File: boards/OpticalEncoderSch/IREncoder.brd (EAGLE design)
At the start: 25.4 x 25.4 mm, 12 parts, among them J1 3_PIN_JST-XH

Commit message: Optical Encoder PCB updates. Awaits peer review and shipment
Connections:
- removed net N$7: J1.P$3
- net GND: now also J1.P$3
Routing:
- net +5V: track 49.8 -> 67.7 mm, vias 2 -> 3
- net N$5: track 7.24 -> 23.2 mm, vias 0 -> 1
- net N$3: track 3.81 -> 4.58 mm
- net N$1: track 3.81 -> 4.58 mm
- added copper zone on layer 1, net GND
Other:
- board text added: "10K"
- board text added: "470"
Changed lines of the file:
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@@
 <hole x="23.495" y="1.905" drill="3.175"/>
 <hole x="23.495" y="23.495" drill="3.175"/>
+<text x="23.622" y="20.066" size="0.508" layer="21">470</text>
+<text x="23.622" y="16.764" size="0.508" layer="21">470</text>
+<text x="0.762" y="8.128" size="0.508" layer="21">470</text>
+<text x="0.762" y="4.826" size="0.508" layer="21">470</text>
+<text x="23.622" y="8.128" size="0.508" layer="21">10K</text>
+<text x="23.622" y="5.08" size="0.508" layer="21">10K</text>
 </plain>
 <attributes>
@@
 <contactref element="R6" pad="2"/>
 <contactref element="J1" pad="P$1"/>
-<wire x1="4.13" y1="5.08" x2="6.03" y2="6.98" width="0.254" layer="1"/>
-<wire x1="6.03" y1="6.98" x2="6.03" y2="8.255" width="0.254" layer="1"/>
-<wire x1="21.27" y1="20.32" x2="19.05" y2="18.1" width="0.254" layer="1"/>
-<wire x1="19.05" y1="18.1" x2="19.05" y2="17.78" width="0.254" layer="1"/>
-<wire x1="4.13" y1="5.08" x2="1.27" y2="5.08" width="0.254" layer="1"/>
 <wire x1="21.27" y1="20.32" x2="22.86" y2="20.32" width="0.254" layer="1"/>
 <via x="22.86" y="20.32" extent="1-16" drill="0.35"/>
-<wire x1="22.86" y1="20.32" x2="22.86" y2="6.35" width="0.254" layer="16"/>
-<wire x1="22.86" y1="6.35" x2="24.13" y2="5.08" width="0.254" layer="16"/>
+<wire x1="22.86" y1="20.32" x2="22.86" y2="5.08" width="0.254" layer="16"/>
 <wire x1="15.24" y1="1.27" x2="19.05" y2="5.08" width="0.254" layer="16"/>
 <wire x1="15.24" y1="1.27" x2="8.89" y2="1.27" width="0.254" layer="16"/>
 <wire x1="8.89" y1="1.27" x2="5.08" y2="5.08" width="0.254" layer="16"/>
-<via x="24.13" y="5.08" extent="1-16" drill="0.35"/>
-<wire x1="19.05" y1="5.08" x2="24.13" y2="5.08" width="0.254" layer="16"/>
-<wire x1="19.05" y1="17.78" x2="19.37" y2="17.145" width="0" layer="19" extent="1-1"/>
-<wire x1="4.13" y1="5.08" x2="5.08" y2="5.08" width="0" layer="19" extent="1-16"/>
-<wire x1="21.27" y1="5.08" x2="19.05" y2="5.08" width="0" layer="19" extent="1-16"/>
-<wire x1="7.845" y1="17.69" x2="6.03" y2="8.255" width="0" layer="19" extent="1-1"/>
+<via x="22.86" y="5.08" extent="1-16" drill="0.35"/>
+<wire x1="19.05" y1="5.08" x2="22.86" y2="5.08" width="0.254" layer="16"/>
+<via x="2.54" y="5.08" extent="1-16" drill="0.35"/>
+<wire x1="2.54" y1="5.08" x2="2.54" y2="14.732" width="0.254" layer="16"/>
+<wire x1="2.54" y1="14.732" x2="5.588" y2="17.78" width="0.254" layer="16"/>
+<wire x1="7.755" y1="17.78" x2="7.845" y2="17.69" width="0.254" layer="16"/>
+<wire x1="5.588" y1="17.78" x2="7.755" y2="17.78" width="0.254" layer="16"/>
+<wire x1="21.27" y1="5.08" x2="22.86" y2="5.08" width="0.254" layer="1"/>
+<wire x1="5.08" y1="5.08" x2="2.54" y2="5.08" width="0.254" layer="16"/>
+<wire x1="4.13" y1="5.08" x2="2.54" y2="5.08" width="0.254" layer="1"/>
+<wire x1="5.842" y1="8.067" x2="6.03" y2="8.255" width="0.254" layer="1"/>
+<wire x1="4.13" y1="5.08" x2="4.318" y2="5.268" width="0.254" layer="1"/>
+<wire x1="4.318" y1="5.268" x2="4.318" y2="6.096" width="0.254" layer="1"/>
+<wire x1="4.318" y1="6.096" x2="5.842" y2="7.62" width="0.254" layer="1"/>
+<wire x1="5.842" y1="7.62" x2="5.842" y2="8.067" width="0.254" layer="1"/>
+<wire x1="19.37" y1="17.145" x2="19.558" y2="17.333" width="0.254" layer="1"/>
+<wire x1="19.558" y1="17.333" x2="19.558" y2="18.288" width="0.254" layer="1"/>
+<wire x1="19.558" y1="18.288" x2="21.27" y2="20" width="0.254" layer="1"/>
+<wire x1="21.27" y1="20" x2="21.27" y2="20.32" width="0.254" layer="1"/>
 </signal>
 <signal name="N$5">
@@
 <contactref element="D5" pad="A"/>
 <contactref element="J1" pad="P$2"/>
-<wire x1="13.97" y1="12.7" x2="18.415" y2="8.255" width="0.254" layer="1"/>
+<wire x1="13.97" y1="12.7" x2="17.018" y2="9.652" width="0.254" layer="1"/>
+<wire x1="17.018" y1="9.652" x2="18.415" y2="8.255" width="0.254" layer="1"/>
 <wire x1="18.415" y1="8.255" x2="19.37" y2="8.255" width="0.254" layer="1"/>
-<wire x1="13.97" y1="12.7" x2="7.845" y2="20.19" width="0" layer="19" extent="1-1"/>
+<via x="17.018" y="9.652" extent="1-16" drill="0.35"/>
+<wire x1="7.845" y1="20.19" x2="11.779" y2="16.256" width="0.254" layer="16"/>
+<wire x1="14.478" y1="16.256" x2="17.018" y2="13.716" width="0.254" layer="16"/>
+<wire x1="17.018" y1="13.716" x2="17.018" y2="9.652" width="0.254" layer="16"/>
+<wire x1="11.779" y1="16.256" x2="14.478" y2="16.256" width="0.254" layer="16"/>
 </signal>
 <signal name="N$6">
@@
 <contactref element="D1" pad="K"/>
 <contactref element="D5" pad="K"/>
-<wire x1="11.43" y1="12.7" x2="19.05" y2="12.7" width="0" layer="19" extent="1-1"/>
-<wire x1="6.35" y1="12.7" x2="11.43" y2="12.7" width="0" layer="19" extent="1-1"/>
-<wire x1="11.43" y1="20.32" x2="11.43" y2="12.7" width="0" layer="19" extent="1-1"/>
-<wire x1="13.97" y1="5.08" x2="11.43" y2="12.7" width="0" layer="19" extent="1-1"/>
+<contactref element="J1" pad="P$3"/>
+<polygon width="0.254" layer="1" isolate="0.4064">
+<vertex x="0" y="25.4"/>
+<vertex x="0" y="0"/>
+<vertex x="25.4" y="0"/>
+<vertex x="25.4" y="25.4"/>
+</polygon>
 </signal>
 <signal name="N$1">
 <contactref element="R4" pad="1"/>
 <contactref element="D4" pad="A"/>
-<wire x1="21.59" y1="12.7" x2="21.59" y2="16.51" width="0.254" layer="1"/>
-<wire x1="21.59" y1="16.51" x2="21.27" y2="17.145" width="0" layer="19" extent="1-1"/>
+<wire x1="21.27" y1="17.145" x2="21.27" y2="13.02" width="0.254" layer="1"/>
+<wire x1="21.27" y1="13.02" x2="21.59" y2="12.7" width="0.254" layer="1"/>
 </signal>
 <signal name="N$2">
@@
 <contactref element="R2" pad="1"/>
 <contactref element="D2" pad="A"/>
-<wire x1="3.81" y1="12.7" x2="3.81" y2="8.89" width="0.254" layer="1"/>
-<wire x1="3.81" y1="8.89" x2="4.13" y2="8.255" width="0" layer="19" extent="1-1"/>
+<wire x1="4.13" y1="8.255" x2="4.13" y2="12.38" width="0.254" layer="1"/>
+<wire x1="4.13" y1="12.38" x2="3.81" y2="12.7" width="0.254" layer="1"/>
 </signal>
 <signal name="N$4">
@@
 <wire x1="11.43" y1="5.08" x2="6.03" y2="5.08" width="0.254" layer="1"/>
 </signal>
-<signal name="N$7">
-<contactref element="J1" pad="P$3"/>
-</signal>
-<signal name="N$8">
-<via x="1.27" y="5.08" extent="1-16" drill="0.35"/>
-</signal>
 </signals>

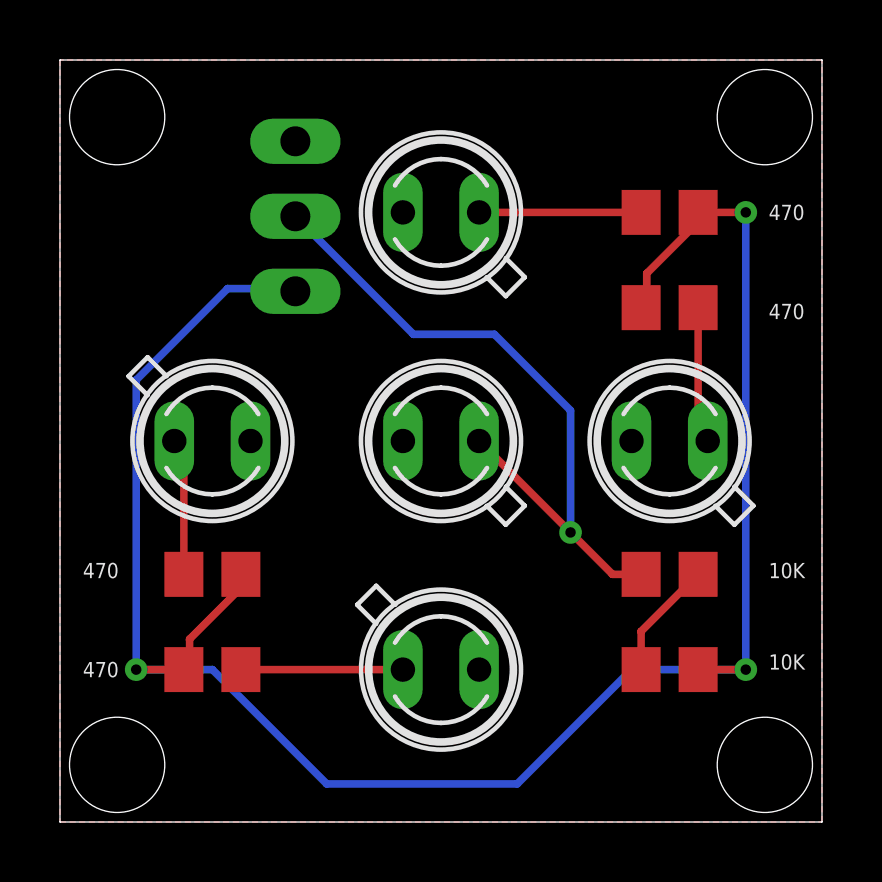
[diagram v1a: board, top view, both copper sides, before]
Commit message: Updating encoder board to fix clearance issues and voltage level
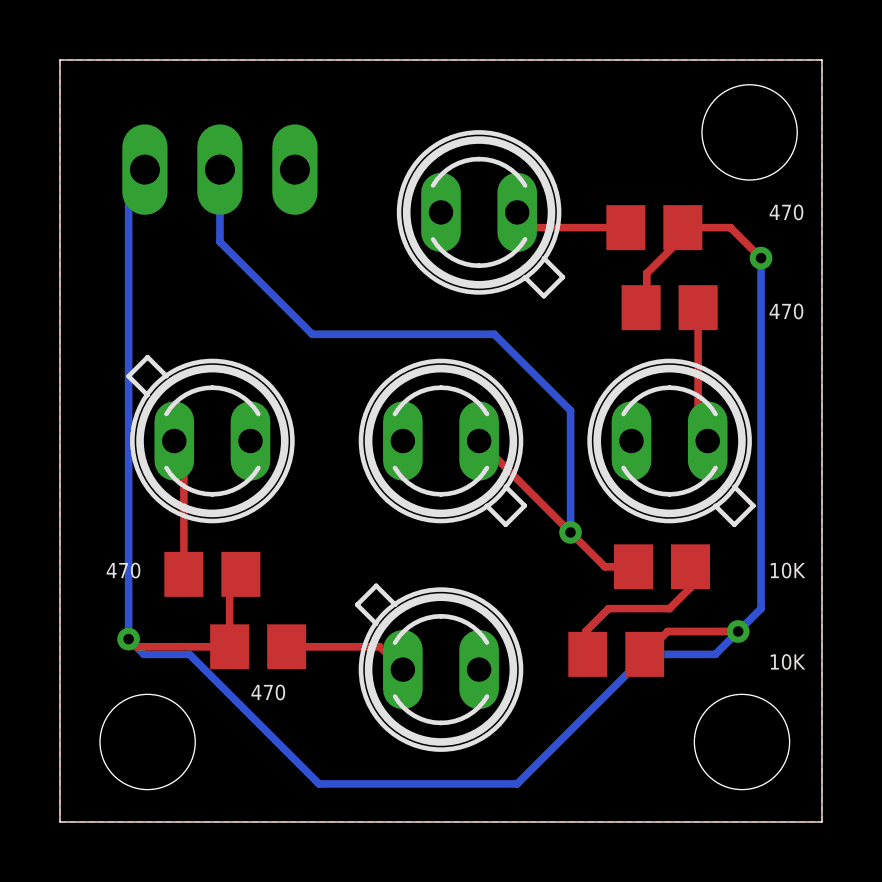
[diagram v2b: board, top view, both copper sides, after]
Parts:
- moved J1 10.7 mm to (0.38, 25.1), turned to 180 degrees
- moved R6 1.85 mm to (18.5, 5.59)
- moved R1 1.70 mm to (6.60, 5.84)
- moved D3 1.27 mm to (14.0, 20.3)
- moved R3 0.72 mm to (19.8, 19.8)
- moved R5 0.36 mm to (20.1, 8.51)
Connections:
- net +5V renamed +3V3
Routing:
- net N$5: track 23.2 -> 27.4 mm
- net +3V3: track 67.7 -> 69.3 mm
- net N$6: track 3.96 -> 5.58 mm
- net N$2: track 5.40 -> 3.83 mm
- net N$4: track 5.40 -> 4.19 mm

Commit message: Cleaning up routing and labels for design review
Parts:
- moved R4 1.27 mm to (21.6, 17.1)
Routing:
- net N$5: track 27.4 -> 21.7 mm, vias 1 -> 0
- net +3V3: track 69.3 -> 69.9 mm
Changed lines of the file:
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@@
 <attribute name="SPICEPREFIX" value="R" x="41.402" y="-4.318" size="1.778" layer="27" display="off"/>
 </element>
-<element name="R4" library="rcl" library_urn="urn:adsk.eagle:library:334" package="R0805" package3d_urn="urn:adsk.eagle:package:23553/2" value="470" x="20.32" y="17.145" smashed="yes" rot="R180">
-<attribute name="SPICEPREFIX" value="R" x="-6.35" y="41.275" size="1.778" layer="27" rot="R180" display="off"/>
+<element name="R4" library="rcl" library_urn="urn:adsk.eagle:library:334" package="R0805" package3d_urn="urn:adsk.eagle:package:23553/2" value="470" x="21.59" y="17.145" smashed="yes" rot="R180">
+<attribute name="SPICEPREFIX" value="R" x="-5.08" y="41.275" size="1.778" layer="27" rot="R180" display="off"/>
 </element>
 <element name="R5" library="rcl" library_urn="urn:adsk.eagle:library:334" package="R0805" package3d_urn="urn:adsk.eagle:package:23553/2" value="10k" x="20.066" y="8.509" smashed="yes">
@@
 <contactref element="D5" pad="A"/>
 <contactref element="J1" pad="P$2"/>
-<wire x1="13.97" y1="12.7" x2="17.018" y2="9.652" width="0.254" layer="1"/>
-<wire x1="17.018" y1="9.652" x2="18.161" y2="8.509" width="0.254" layer="1"/>
+<wire x1="13.97" y1="12.7" x2="18.161" y2="8.509" width="0.254" layer="1"/>
 <wire x1="18.161" y1="8.509" x2="19.116" y2="8.509" width="0.254" layer="1"/>
-<via x="17.018" y="9.652" extent="1-16" drill="0.35"/>
-<wire x1="14.478" y1="16.256" x2="17.018" y2="13.716" width="0.254" layer="16"/>
-<wire x1="17.018" y1="13.716" x2="17.018" y2="9.652" width="0.254" layer="16"/>
-<wire x1="14.478" y1="16.256" x2="8.41168125" y2="16.256" width="0.254" layer="16"/>
-<wire x1="8.41168125" y1="16.256" x2="5.331" y2="19.33668125" width="0.254" layer="16"/>
+<wire x1="5.331" y1="19.33668125" x2="8.41168125" y2="16.256" width="0.254" layer="16"/>
 <wire x1="5.331" y1="19.33668125" x2="5.331" y2="21.746" width="0.254" layer="16"/>
+<wire x1="8.41168125" y1="16.256" x2="12.192" y2="16.256" width="0.254" layer="16"/>
+<wire x1="12.192" y1="16.256" x2="13.97" y2="14.478" width="0.254" layer="16"/>
+<wire x1="13.97" y1="14.478" x2="13.97" y2="12.7" width="0.254" layer="16"/>
 </signal>
 <signal name="N$6">
@@
 <contactref element="R4" pad="1"/>
 <contactref element="D4" pad="A"/>
-<wire x1="21.27" y1="17.145" x2="21.27" y2="13.02" width="0.254" layer="1"/>
-<wire x1="21.27" y1="13.02" x2="21.59" y2="12.7" width="0.254" layer="1"/>
+<wire x1="22.54" y1="17.145" x2="22.54" y2="13.65" width="0.254" layer="1"/>
+<wire x1="21.59" y1="12.7" x2="22.54" y2="13.65" width="0.254" layer="1"/>
 </signal>
 <signal name="N$2">
@@
 <contactref element="R2" pad="2"/>
 <contactref element="R1" pad="2"/>
-<wire x1="19.37" y1="17.145" x2="19.558" y2="17.333" width="0.254" layer="1"/>
-<wire x1="19.558" y1="17.333" x2="19.558" y2="18.288" width="0.254" layer="1"/>
-<wire x1="19.558" y1="18.288" x2="20.762" y2="19.492" width="0.254" layer="1"/>
-<wire x1="20.762" y1="19.492" x2="20.762" y2="19.812" width="0.254" layer="1"/>
+<wire x1="20.762" y1="17.9862" x2="20.64" y2="17.785" width="0.254" layer="1"/>
+<wire x1="20.64" y1="17.145" x2="20.64" y2="17.785" width="0.254" layer="1"/>
+<wire x1="20.762" y1="17.9862" x2="20.762" y2="19.812" width="0.254" layer="1"/>
 <wire x1="5.654" y1="5.842" x2="5.654" y2="7.879" width="0.254" layer="1"/>
 <wire x1="5.654" y1="7.879" x2="6.03" y2="8.255" width="0.254" layer="1"/>
@@
 <wire x1="15.24" y1="1.27" x2="19.558" y2="5.588" width="0.254" layer="16"/>
 <wire x1="15.24" y1="1.27" x2="8.636" y2="1.27" width="0.254" layer="16"/>
-<wire x1="8.636" y1="1.27" x2="4.318" y2="5.588" width="0.254" layer="16"/>
-<wire x1="4.318" y1="5.588" x2="2.794" y2="5.588" width="0.254" layer="16"/>
-<wire x1="2.794" y1="5.588" x2="2.286" y2="6.096" width="0.254" layer="16"/>
+<wire x1="8.636" y1="1.27" x2="4.064" y2="5.842" width="0.254" layer="16"/>
+<wire x1="4.064" y1="5.842" x2="2.794" y2="5.842" width="0.254" layer="16"/>
+<wire x1="2.794" y1="5.842" x2="1.778" y2="6.858" width="0.254" layer="16"/>
 <via x="22.606" y="6.35" extent="1-16" drill="0.35"/>
 <wire x1="21.844" y1="5.588" x2="22.606" y2="6.35" width="0.254" layer="16"/>
 <wire x1="21.844" y1="5.588" x2="19.558" y2="5.588" width="0.254" layer="16"/>
-<via x="2.286" y="6.096" extent="1-16" drill="0.35"/>
-<wire x1="22.606" y1="6.35" x2="20.254" y2="6.35" width="0.254" layer="1"/>
+<via x="1.778" y="6.858" extent="1-16" drill="0.35"/>
+<wire x1="22.606" y1="6.35" x2="21.844" y2="5.588" width="0.254" layer="1"/>
+<wire x1="21.844" y1="5.588" x2="19.492" y2="5.588" width="0.254" layer="1"/>
 <wire x1="6.03" y1="8.26" x2="5.654" y2="8.636" width="0.254" layer="1"/>
-<wire x1="2.286" y1="21.201" x2="2.831" y2="21.746" width="0.254" layer="16"/>
-<wire x1="2.286" y1="6.096" x2="2.286" y2="21.201" width="0.254" layer="16"/>
-<wire x1="20.254" y1="6.35" x2="19.492" y2="5.588" width="0.254" layer="1"/>
+<wire x1="1.778" y1="20.693" x2="2.831" y2="21.746" width="0.254" layer="16"/>
+<wire x1="1.778" y1="6.858" x2="1.778" y2="20.693" width="0.254" layer="16"/>
 <wire x1="22.352" y1="19.812" x2="20.762" y2="19.812" width="0.254" layer="1"/>
-<wire x1="2.286" y1="6.096" x2="2.54" y2="5.842" width="0.254" layer="1"/>
-<wire x1="2.54" y1="5.842" x2="5.654" y2="5.842" width="0.254" layer="1"/>
+<wire x1="1.778" y1="6.858" x2="2.794" y2="5.842" width="0.254" layer="1"/>
+<wire x1="2.794" y1="5.842" x2="5.654" y2="5.842" width="0.254" layer="1"/>
 <wire x1="6.03" y1="8.255" x2="6.03" y2="8.26" width="0" layer="19" extent="1-1"/>
 </signal>
